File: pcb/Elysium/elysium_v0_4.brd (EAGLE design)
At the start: 64.8 x 105.1 mm, 20 parts, among them U1 TLC5940-NT, U2 TLC5940-NT, U3 TLC5940-NT, U4 TLC5940-NT

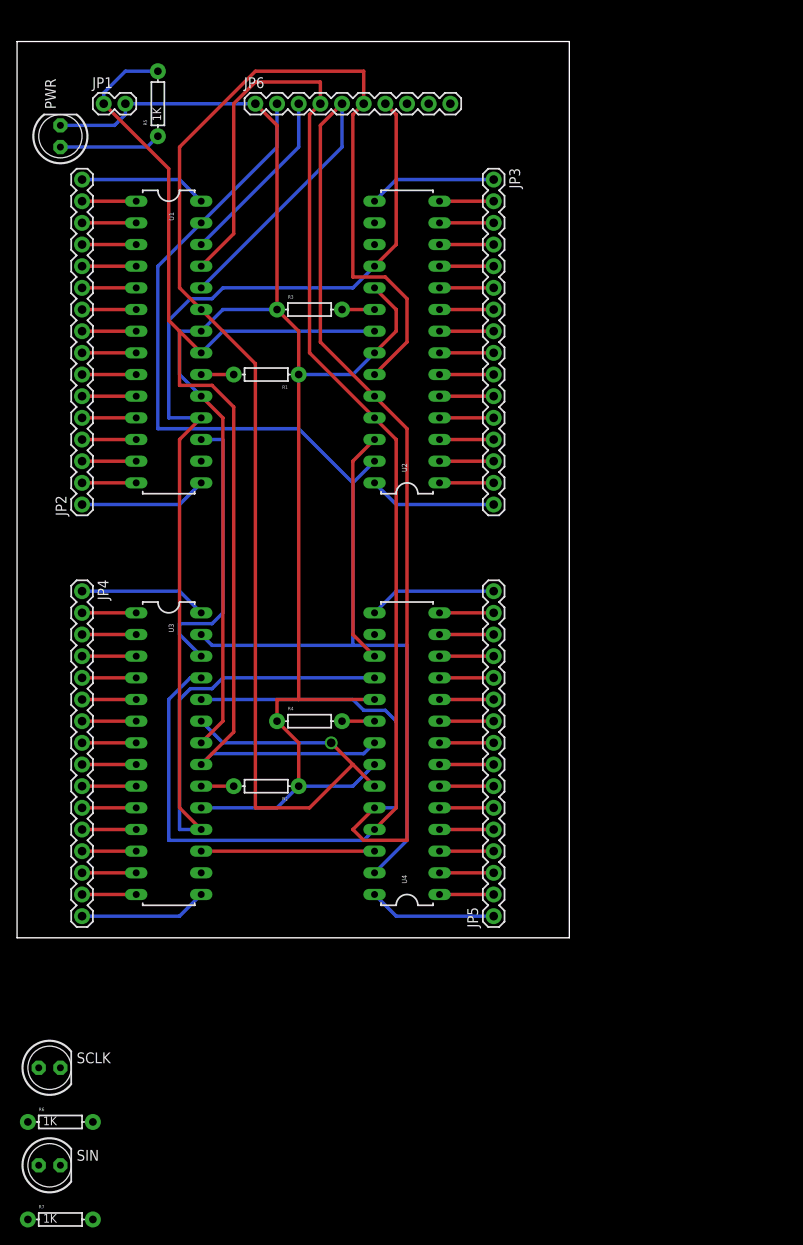
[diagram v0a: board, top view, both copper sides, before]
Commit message: Added rev_0_4 board
Rev 0_4 has status LEDs with ground planes.
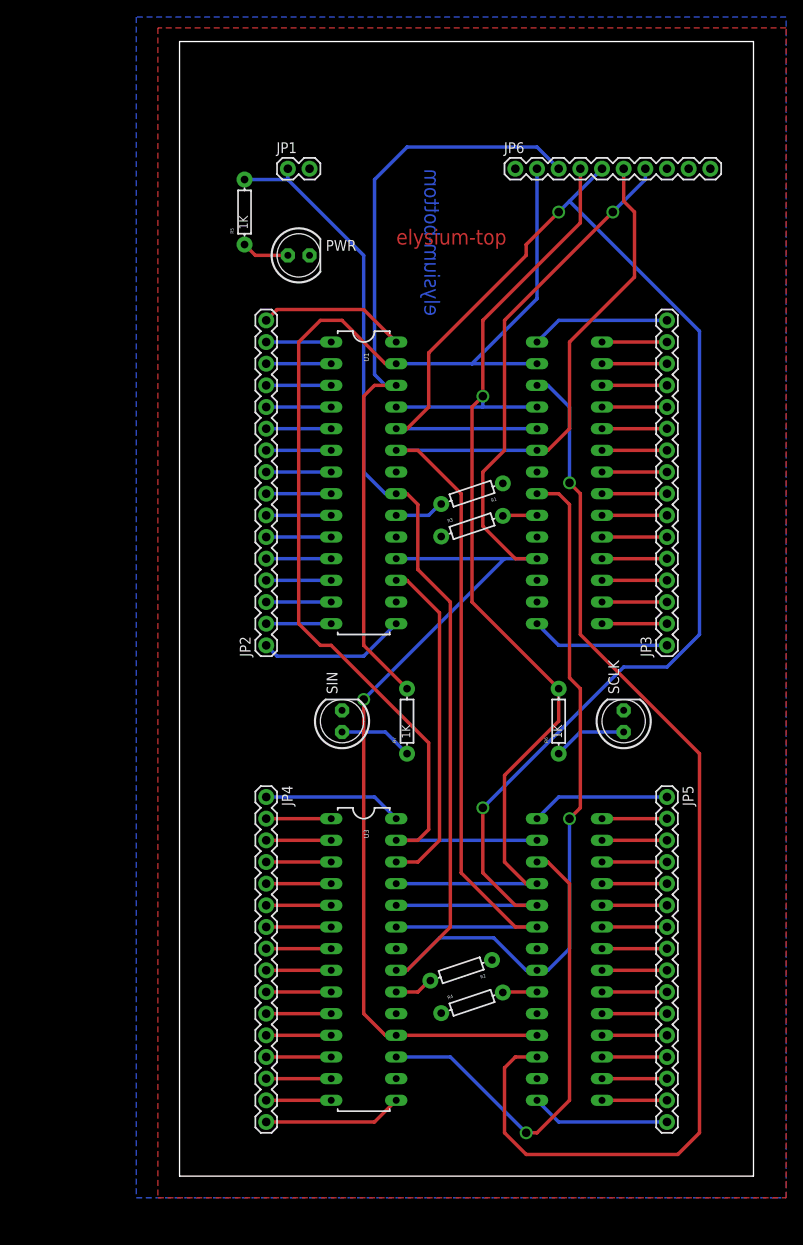
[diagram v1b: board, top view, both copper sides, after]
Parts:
- moved SCLK 78.6 mm to (71.1, 20.3), turned to 90 degrees
- moved R6 75.0 mm to (63.5, 20.3), turned to 90 degrees
- moved R7 71.2 mm to (45.7, 20.3), turned to 90 degrees
- moved SIN 62.3 mm to (38.1, 20.3), turned to 90 degrees
- moved JP3 58.3 mm to (76.2, 29.2), turned to 90 degrees
- moved R4 38.1 mm to (53.3, -12.7), turned to 18.5 degrees
- moved U3 33.2 mm to (40.6, -7.62)
- moved JP4 32.4 mm to (29.2, 11.4)
- moved R3 31.8 mm to (53.3, 43.2), turned to 18.5 degrees
- moved R2 31.4 mm to (52.1, -8.89), turned to 198.5 degrees
- moved JP6 31.4 mm to (58.4, 85.1)
- moved PWR 31.2 mm to (33.0, 74.9), turned to 0 degrees
- moved U4 30.7 mm to (64.8, -7.62), flipped to the bottom, turned to 270 degrees
- moved U1 28.2 mm to (40.6, 48.3)
- moved R1 27.9 mm to (53.3, 47.0), turned to 198.5 degrees
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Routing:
- net GND: track 225.2 -> 0.00 mm
- net N$67: track 27.5 -> 133.2 mm, vias 0 -> 1
- net SIN: track 21.2 -> 90.9 mm
- net VCC: track 142.6 -> 193.8 mm, vias 0 -> 1
- net BLANK: track 186.0 -> 137.7 mm, vias 1 -> 0
- net SCLK: track 171.3 -> 132.5 mm, vias 0 -> 1
- net N$66: track 20.3 -> 55.8 mm, vias 0 -> 1
- net XLAT: track 167.1 -> 180.7 mm, vias 0 -> 2
- net N$74: track 0.00 -> 8.67 mm
- net N$76: track 0.00 -> 8.67 mm
- net N$69: track 12.0 -> 5.61 mm
- net N$65: track 33.3 -> 39.5 mm
- net VPRG: track 144.9 -> 142.2 mm
- net N$1: track 15.0 -> 17.3 mm
- net N$16: track 15.0 -> 17.3 mm
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- added copper zone on layer 1, net GND
- added copper zone on layer 16, net GND
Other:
- board size 64.8 x 105.1 mm -> 67.3 x 133 mm
- board text added: "elysium-bottom"
- board text added: "elysium-top"
